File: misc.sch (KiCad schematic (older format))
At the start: 39 parts, among them J13 MICROSD_SLOT_TFP09-2-12B, P13 EXT_SD, P14 LCD, P15 LIMIT_SWITCHES, P16 LIMIT_SWITCHES_V, P17 CONN_01X03, P18 CONN_01X03, P19 CONN_01X03, P20 CONN_01X03, P21 THERMISTORS, P22 CONN_01X05, SW1 RESET, U2 24LC256

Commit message: cleanup
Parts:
- SW1: footprint armin-footprints:BUTTON_PUSH_SMD_6x6mm -> buttons_switches:BUTTON_PUSH_SMD_6x6mm
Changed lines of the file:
@@
 F 0 "SW1" H 5350 5206 50  0000 C CNN
 F 1 "RESET" H 5350 5114 50  0000 C CNN
-F 2 "armin-footprints:BUTTON_PUSH_SMD_6x6mm" H 5350 4950 50  0001 C CNN
+F 2 "buttons_switches:BUTTON_PUSH_SMD_6x6mm" H 5350 4950 50  0001 C CNN
 F 3 "" H 5350 4950 50  0000 C CNN
 	1    5350 4950

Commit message: fixed minor issue
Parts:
- P13, P14, P21: footprint armin-footprints:CON_HDR_2x5_2.54mm -> headers:CON_HDR_2x5_2.54mm
- P15: footprint armin-footprints:CON_HDR_2x7_2.54mm -> headers:CON_HDR_2x7_2.54mm
- P16: footprint armin-footprints:CON_HDR_1x7_2.54mm -> headers:CON_HDR_1x7_2.54mm
- P17, P18, P19, P20: footprint armin-footprints:CON_HDR_1x3_2.54mm -> headers:CON_HDR_1x3_2.54mm
- P22: footprint armin-footprints:CON_HDR_1x5_2.54mm -> headers:CON_HDR_1x5_2.54mm
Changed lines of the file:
@@
 F 0 "P21" H 9700 2216 50  0000 C CNN
 F 1 "THERMISTORS" H 9700 2124 50  0000 C CNN
-F 2 "armin-footprints:CON_HDR_2x5_2.54mm" H 9700 600 50  0001 C CNN
+F 2 "headers:CON_HDR_2x5_2.54mm" H 9700 600 50  0001 C CNN
 F 3 "" H 9700 600 50  0000 C CNN
 	1    9700 1800
@@
 F 0 "P22" H 10527 1838 50  0000 L CNN
 F 1 "CONN_01X05" H 10527 1746 50  0000 L CNN
-F 2 "armin-footprints:CON_HDR_1x5_2.54mm" H 10450 1800 50  0001 C CNN
+F 2 "headers:CON_HDR_1x5_2.54mm" H 10450 1800 50  0001 C CNN
 F 3 "" H 10450 1800 50  0000 C CNN
 	1    10450 1800
@@
 F 0 "P15" H 6225 2300 50  0000 C CNN
 F 1 "LIMIT_SWITCHES" H 6100 2225 50  0000 C CNN
-F 2 "armin-footprints:CON_HDR_2x7_2.54mm" H 6225 625 50  0001 C CNN
+F 2 "headers:CON_HDR_2x7_2.54mm" H 6225 625 50  0001 C CNN
 F 3 "" H 6225 625 50  0000 C CNN
 	1    6225 1825
@@
 F 0 "P16" H 7177 1863 50  0000 L CNN
 F 1 "LIMIT_SWITCHES_V" H 7177 1771 50  0000 L CNN
-F 2 "armin-footprints:CON_HDR_1x7_2.54mm" H 7100 1825 50  0001 C CNN
+F 2 "headers:CON_HDR_1x7_2.54mm" H 7100 1825 50  0001 C CNN
 F 3 "" H 7100 1825 50  0000 C CNN
 	1    7100 1825
@@
 F 0 "P20" H 7425 4550 50  0000 L CNN
 F 1 "CONN_01X03" H 6975 4750 50  0000 L CNN
-F 2 "armin-footprints:CON_HDR_1x3_2.54mm" H 7325 4550 50  0001 C CNN
+F 2 "headers:CON_HDR_1x3_2.54mm" H 7325 4550 50  0001 C CNN
 F 3 "" H 7325 4550 50  0000 C CNN
 	1    7325 4550
@@
 F 0 "P19" H 7425 4050 50  0000 L CNN
 F 1 "CONN_01X03" H 6975 4250 50  0000 L CNN
-F 2 "armin-footprints:CON_HDR_1x3_2.54mm" H 7325 4050 50  0001 C CNN
+F 2 "headers:CON_HDR_1x3_2.54mm" H 7325 4050 50  0001 C CNN
 F 3 "" H 7325 4050 50  0000 C CNN
 	1    7325 4050
@@
 F 0 "P18" H 7425 3550 50  0000 L CNN
 F 1 "CONN_01X03" H 6975 3750 50  0000 L CNN
-F 2 "armin-footprints:CON_HDR_1x3_2.54mm" H 7325 3550 50  0001 C CNN
+F 2 "headers:CON_HDR_1x3_2.54mm" H 7325 3550 50  0001 C CNN
 F 3 "" H 7325 3550 50  0000 C CNN
 	1    7325 3550
@@
 F 0 "P17" H 7425 3050 50  0000 L CNN
 F 1 "CONN_01X03" H 6975 3250 50  0000 L CNN
-F 2 "armin-footprints:CON_HDR_1x3_2.54mm" H 7325 3050 50  0001 C CNN
+F 2 "headers:CON_HDR_1x3_2.54mm" H 7325 3050 50  0001 C CNN
 F 3 "" H 7325 3050 50  0000 C CNN
 	1    7325 3050
@@
 F 0 "P13" H 2400 6291 50  0000 C CNN
 F 1 "EXT_SD" H 2400 6199 50  0000 C CNN
-F 2 "armin-footprints:CON_HDR_2x5_2.54mm" H 2400 4675 50  0001 C CNN
+F 2 "headers:CON_HDR_2x5_2.54mm" H 2400 4675 50  0001 C CNN
 F 3 "" H 2400 4675 50  0000 C CNN
 	1    2400 5875
@@
 F 0 "P14" H 2400 7341 50  0000 C CNN
 F 1 "LCD" H 2400 7249 50  0000 C CNN
-F 2 "armin-footprints:CON_HDR_2x5_2.54mm" H 2400 5725 50  0001 C CNN
+F 2 "headers:CON_HDR_2x5_2.54mm" H 2400 5725 50  0001 C CNN
 F 3 "" H 2400 5725 50  0000 C CNN
 	1    2400 6925

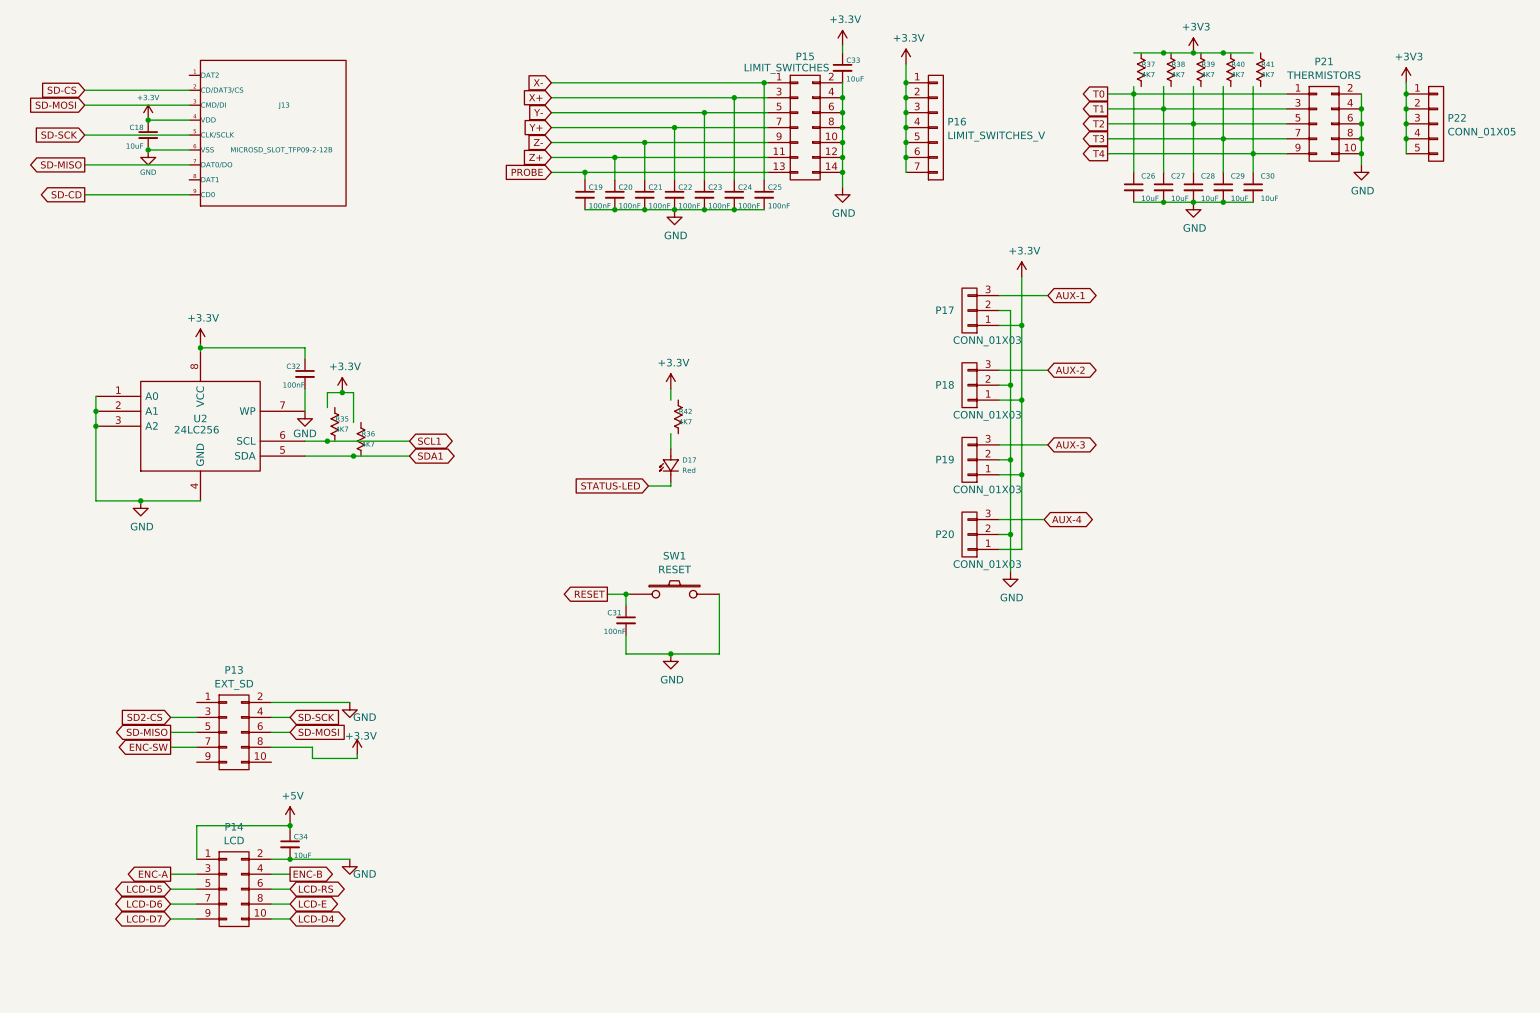
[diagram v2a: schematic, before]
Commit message: - added wifi esp8266 - switched caps to smd - fixed dual transistor pinout bug
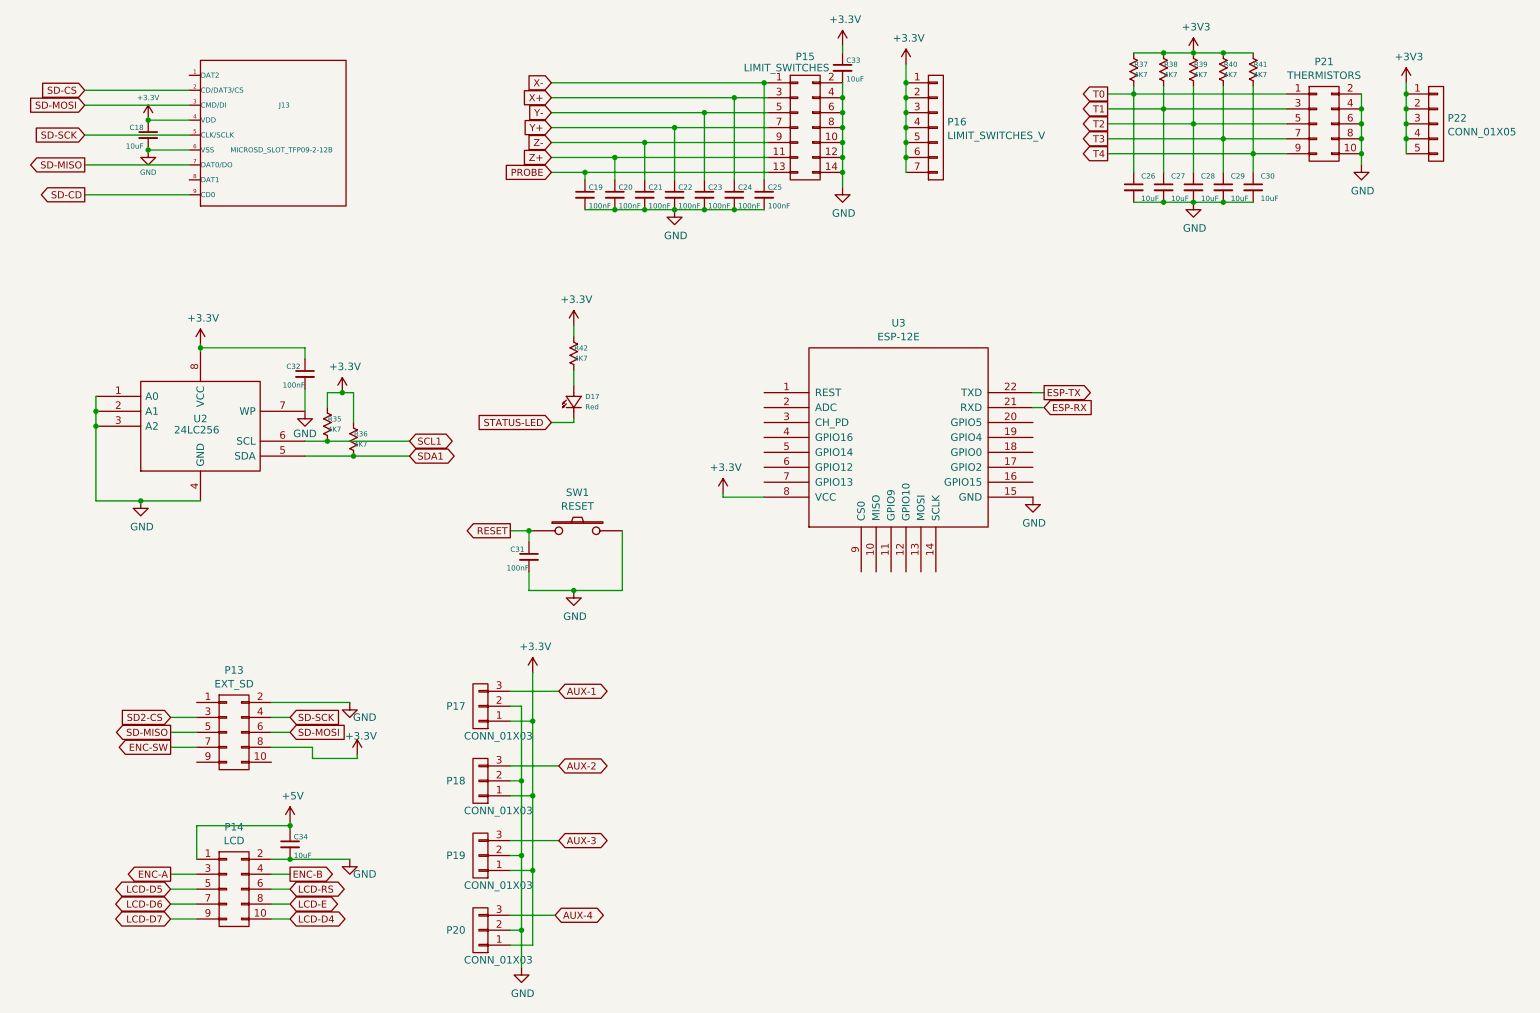
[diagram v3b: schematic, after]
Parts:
- added U3: ESP-12E, misc:ESP-12E, symbol ESP-12E
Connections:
- net labels added: ESP-RX, ESP-TX
- wire segments 95 -> 99
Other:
- moved on the sheet: C31, D17, P17, P18, P19, P20, R35, R36, R37, R38, R39, R40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

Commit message: some refinements
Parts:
- R42: value 4K7 -> 470R
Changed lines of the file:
@@
 U 1 1 568F903C
 P 4600 3225
-F 0 "R42" V 4677 3303 34  0000 L CNN
-F 1 "4K7" V 4746 3303 34  0000 L CNN
+F 0 "R42" V 4650 3325 34  0000 L CNN
+F 1 "470R" V 4750 3325 34  0000 L CNN
 F 2 "resistors:R_0603" H 4600 3225 60  0001 C CNN
 F 3 "" H 4600 3225 60  0000 C CNN

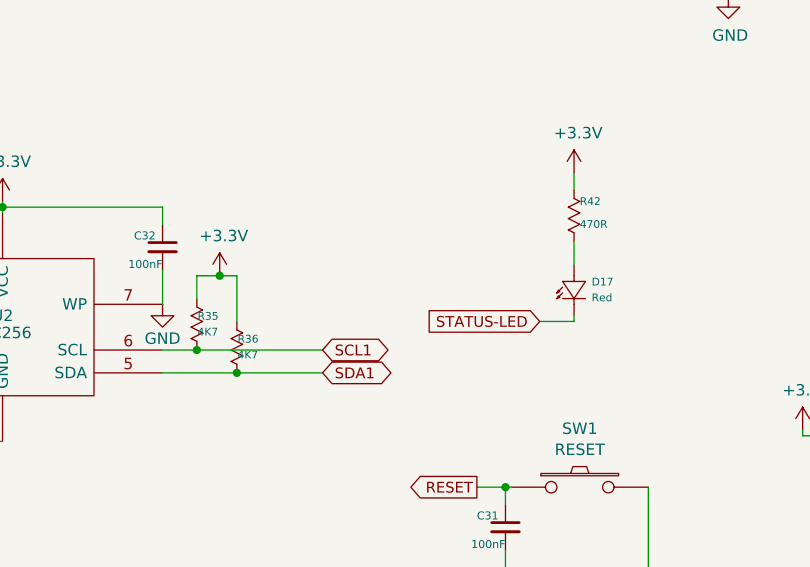
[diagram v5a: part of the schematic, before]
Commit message: - Some mosfets now can have hardware PWM - moved eeprom to i2c with arduino pull-ups
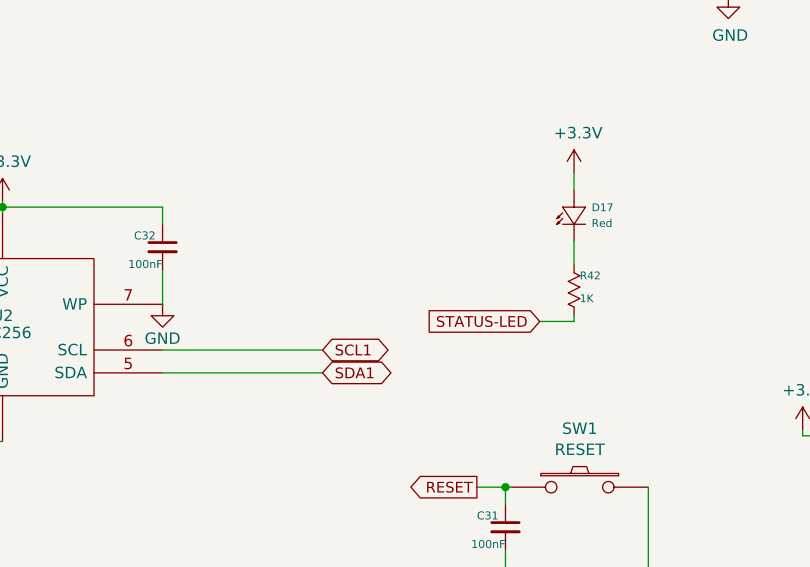
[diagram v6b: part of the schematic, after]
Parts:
- removed R35, R36: 4K7, resistors:R_0603, symbol RESISTOR
- R42: value 470R -> 1K
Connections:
- net +3V3: now also D17.1 (null); no longer R42.1
- net STATUS-LED: now also R42.2; no longer D17.2 (null)
- new net: D17.2 (null), R42.1
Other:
- moved on the sheet: D17, R42
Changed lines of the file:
@@
-	1    0    0    -1
-$EndComp
-$Comp
-L RESISTOR R36
-U 1 1 568E7F50
-P 3125 3800
-F 0 "R36" V 3202 3878 34  0000 L CNN
-F 1 "4K7" V 3271 3878 34  0000 L CNN
-F 2 "resistors:R_0603" H 3125 3800 60  0001 C CNN
-F 3 "" H 3125 3800 60  0000 C CNN
-	1    3125 3800
-	0    1    1    0
-$EndComp
-$Comp
-L RESISTOR R35
-U 1 1 568E81EE
-P 2950 3700
-F 0 "R35" V 3027 3778 34  0000 L CNN
-F 1 "4K7" V 3096 3778 34  0000 L CNN
-F 2 "resistors:R_0603" H 2950 3700 60  0001 C CNN
-F 3 "" H 2950 3700 60  0000 C CNN
-	1    2950 3700
-	0    1    1    0
-$EndComp
-$Comp
-L +3.3V #PWR71
-U 1 1 568E82EF
-P 3125 3600
-F 0 "#PWR71" H 3125 3450 50  0001 C CNN
-F 1 "+3.3V" H 3143 3774 50  0000 C CNN
-F 2 "" H 3125 3600 50  0000 C CNN
-F 3 "" H 3125 3600 50  0000 C CNN
-	1    3125 3600
 	1    0    0    -1
 $EndComp
@@
 Connection ~ 5750 2375
 Wire Wire Line
-	3025 3700 3025 3600
-Wire Wire Line
-	3025 3600 3200 3600
-Wire Wire Line
-	3200 3600 3200 3800
-Wire Wire Line
 	2875 3925 3575 3925
 Wire Wire Line
 	2875 4025 3575 4025
-Connection ~ 3025 3925
-Connection ~ 3200 4025
 $Comp
 L CONN_01X03 P19
@@
 L Red D17
 U 1 1 568F7EEA
-P 4725 3775
-F 0 "D17" V 4873 3748 34  0000 R CNN
-F 1 "Red" V 4804 3748 34  0000 R CNN
-F 2 "diodes:LED-0603" H 4725 3775 60  0001 C CNN
-F 3 "" H 4725 3775 60  0000 C CNN
-	1    4725 3775
+P 4725 3450
+F 0 "D17" V 4873 3423 34  0000 R CNN
+F 1 "Red" V 4804 3423 34  0000 R CNN
+F 2 "diodes:LED-0603" H 4725 3450 60  0001 C CNN
+F 3 "" H 4725 3450 60  0000 C CNN
+	1    4725 3450
 	0    -1   -1   0
 $EndComp
@@
 L RESISTOR R42
 U 1 1 568F903C
-P 4600 3225
-F 0 "R42" V 4650 3325 34  0000 L CNN
-F 1 "470R" V 4750 3325 34  0000 L CNN
-F 2 "resistors:R_0603" H 4600 3225 60  0001 C CNN
-F 3 "" H 4600 3225 60  0000 C CNN
-	1    4600 3225
+P 4600 3550
+F 0 "R42" V 4650 3650 34  0000 L CNN
+F 1 "1K" V 4750 3650 34  0000 L CNN
+F 2 "resistors:R_0603" H 4600 3550 60  0001 C CNN
+F 3 "" H 4600 3550 60  0000 C CNN
+	1    4600 3550
 	0    1    1    0
 $EndComp
@@
 Connection ~ 4400 5800
 Connection ~ 4325 7200
-Connection ~ 3125 3600
 $Comp
 L C_Small C33

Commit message: Fixed some TODO's
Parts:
- added C36: 10uF, capacitors:C_0805, symbol C_Small
- added P25: CONN_01X03, headers:CON_HDR_1x3_2.54mm, symbol CONN_01X03
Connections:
- net +3V3: now also C36.1
- net GND: now also C36.2, P25.1 (P1)
- net SCL1: now also P25.3 (P3)
- net SDA1: now also P25.2 (P2)
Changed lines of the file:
@@
 $EndComp
 $Comp
-L GND #PWR87
+L GND #PWR88
 U 1 1 568D834C
 P 9950 2075
-F 0 "#PWR87" H 9950 1825 50  0001 C CNN
+F 0 "#PWR88" H 9950 1825 50  0001 C CNN
 F 1 "GND" H 9958 1901 50  0000 C CNN
 F 2 "" H 9950 2075 50  0000 C CNN
@@
 $EndComp
 $Comp
-L GND #PWR86
+L GND #PWR87
 U 1 1 568D94E5
 P 8825 2325
-F 0 "#PWR86" H 8825 2075 50  0001 C CNN
+F 0 "#PWR87" H 8825 2075 50  0001 C CNN
 F 1 "GND" H 8833 2151 50  0000 C CNN
 F 2 "" H 8825 2325 50  0000 C CNN
@@
 $EndComp
 $Comp
-L +3V3 #PWR85
+L +3V3 #PWR86
 U 1 1 568D9512
 P 8825 1325
-F 0 "#PWR85" H 8825 1175 50  0001 C CNN
+F 0 "#PWR86" H 8825 1175 50  0001 C CNN
 F 1 "+3V3" H 8843 1499 50  0000 C CNN
 F 2 "" H 8825 1325 50  0000 C CNN
@@
 $EndComp
 $Comp
-L +3V3 #PWR88
+L +3V3 #PWR89
 U 1 1 568D9A56
 P 10250 1525
-F 0 "#PWR88" H 10250 1375 50  0001 C CNN
+F 0 "#PWR89" H 10250 1375 50  0001 C CNN
 F 1 "+3V3" H 10268 1699 50  0000 C CNN
 F 2 "" H 10250 1525 50  0000 C CNN
@@
 $EndComp
 $Comp
-L GND #PWR70
+L GND #PWR71
 U 1 1 568DA443
 P 2875 3725
-F 0 "#PWR70" H 2875 3475 50  0001 C CNN
+F 0 "#PWR71" H 2875 3475 50  0001 C CNN
 F 1 "GND" H 2875 3575 50  0000 C CNN
 F 2 "" H 2875 3725 50  0000 C CNN
@@
 $EndComp
 $Comp
-L GND #PWR82
+L GND #PWR83
 U 1 1 568D90A7
 P 6475 2225
-F 0 "#PWR82" H 6475 1975 50  0001 C CNN
+F 0 "#PWR83" H 6475 1975 50  0001 C CNN
 F 1 "GND" H 6483 2051 50  0000 C CNN
 F 2 "" H 6475 2225 50  0000 C CNN
@@
 $EndComp
 $Comp
-L +3.3V #PWR83
+L +3.3V #PWR84
 U 1 1 568D9133
 P 6900 1400
-F 0 "#PWR83" H 6900 1250 50  0001 C CNN
+F 0 "#PWR84" H 6900 1250 50  0001 C CNN
 F 1 "+3.3V" H 6918 1574 50  0000 C CNN
 F 2 "" H 6900 1400 50  0000 C CNN
@@
 	3225 6050 3225 6025
 $Comp
-L +5V #PWR69
+L +5V #PWR70
 U 1 1 568F17B3
 P 2775 6475
-F 0 "#PWR69" H 2775 6325 50  0001 C CNN
+F 0 "#PWR70" H 2775 6325 50  0001 C CNN
 F 1 "+5V" H 2793 6649 50  0000 C CNN
 F 2 "" H 2775 6475 50  0000 C CNN
@@
 $EndComp
 $Comp
-L +3.3V #PWR81
+L +3.3V #PWR82
 U 1 1 56944144
 P 6475 1275
-F 0 "#PWR81" H 6475 1125 50  0001 C CNN
+F 0 "#PWR82" H 6475 1125 50  0001 C CNN
 F 1 "+3.3V" H 6493 1449 50  0000 C CNN
 F 2 "" H 6475 1275 50  0000 C CNN
@@
 	5675 4300 5675 4275
 $Comp
-L GND #PWR84
+L GND #PWR85
 U 1 1 56BB74F0
 P 7750 4300
-F 0 "#PWR84" H 7750 4050 50  0001 C CNN
+F 0 "#PWR85" H 7750 4050 50  0001 C CNN
 F 1 "GND" H 7758 4126 50  0000 C CNN
 F 2 "" H 7750 4300 50  0000 C CNN
@@
 Wire Wire Line
 	7750 3700 7825 3700
+$Comp
+L CONN_01X03 P25
+U 1 1 56C3648D
+P 2375 4850
+F 0 "P25" H 2294 4518 50  0000 C CNN
+F 1 "CONN_01X03" H 2294 4610 50  0000 C CNN
+F 2 "headers:CON_HDR_1x3_2.54mm" H 2375 4850 50  0001 C CNN
+F 3 "" H 2375 4850 50  0000 C CNN
+	1    2375 4850
+	-1   0    0    1
+$EndComp
+Text GLabel 2700 4750 2    47   BiDi ~ 0
+SCL1
+Text GLabel 2700 4850 2    47   BiDi ~ 0
+SDA1
+Wire Wire Line
+	2575 4750 2700 4750
+Wire Wire Line
+	2700 4850 2575 4850
+$Comp
+L GND #PWR69
+U 1 1 56C36C49
+P 2575 4950
+F 0 "#PWR69" H 2575 4700 50  0001 C CNN
+F 1 "GND" H 2575 4800 50  0000 C CNN
+F 2 "" H 2575 4950 50  0000 C CNN
+F 3 "" H 2575 4950 50  0000 C CNN
+	1    2575 4950
+	1    0    0    -1
+$EndComp
+$Comp
+L C_Small C36
+U 1 1 56C38BB3
+P 5900 4400
+F 0 "C36" H 5775 4450 35  0000 L CNN
+F 1 "10uF" H 5750 4325 35  0000 L CNN
+F 2 "capacitors:C_0805" H 5900 4400 50  0001 C CNN
+F 3 "" H 5900 4400 50  0000 C CNN
+	1    5900 4400
+	1    0    0    -1
+$EndComp
+$Comp
+L GND #PWR81
+U 1 1 56C38FAF
+P 5900 4550
+F 0 "#PWR81" H 5900 4300 50  0001 C CNN
+F 1 "GND" H 5908 4376 50  0000 C CNN
+F 2 "" H 5900 4550 50  0000 C CNN
+F 3 "" H 5900 4550 50  0000 C CNN
+	1    5900 4550
+	1    0    0    -1
+$EndComp
+Connection ~ 5900 4300
+Wire Wire Line
+	5900 4550 5900 4500
 $EndSCHEMATC
